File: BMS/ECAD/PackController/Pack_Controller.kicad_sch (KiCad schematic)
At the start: 0 parts

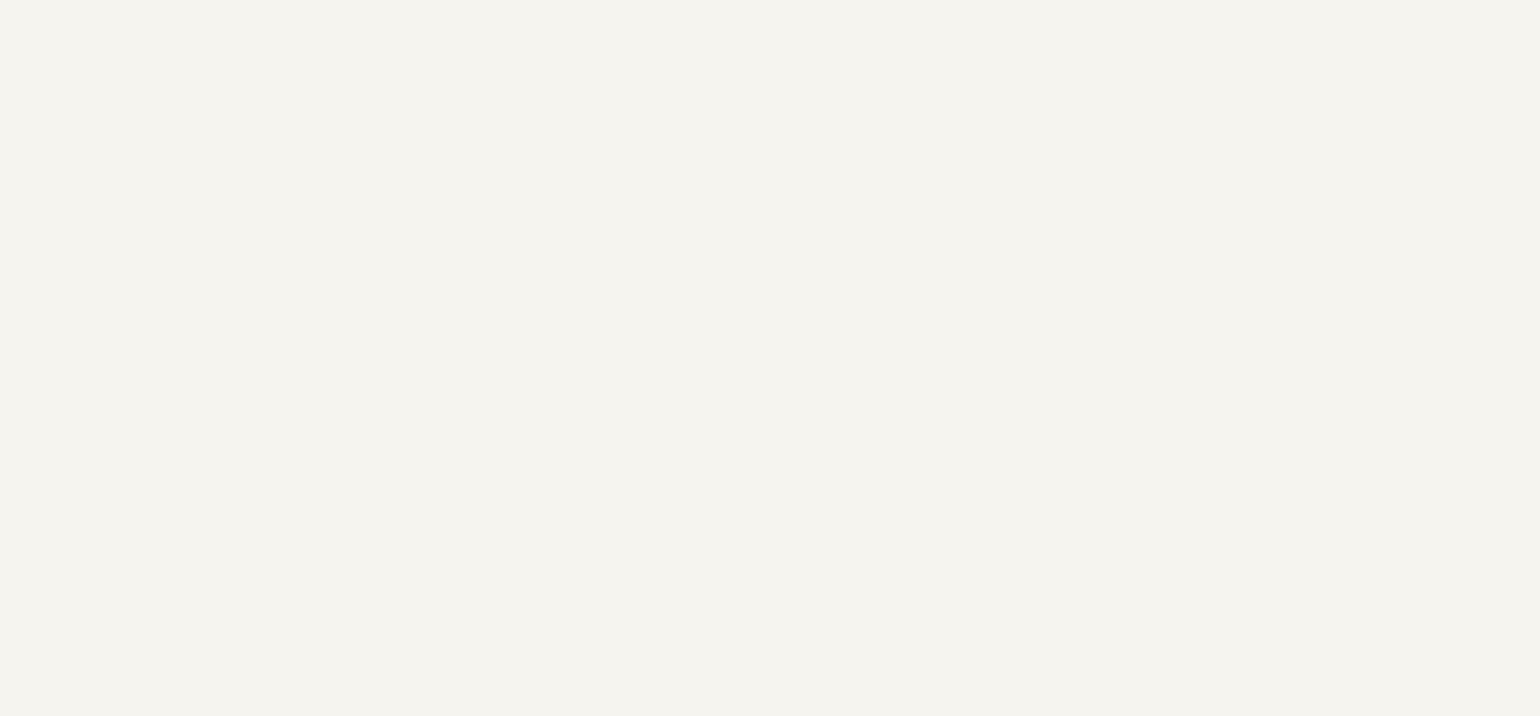
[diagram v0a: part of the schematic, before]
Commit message: did AIR monitoring circuit and started SDC CTRL / logik
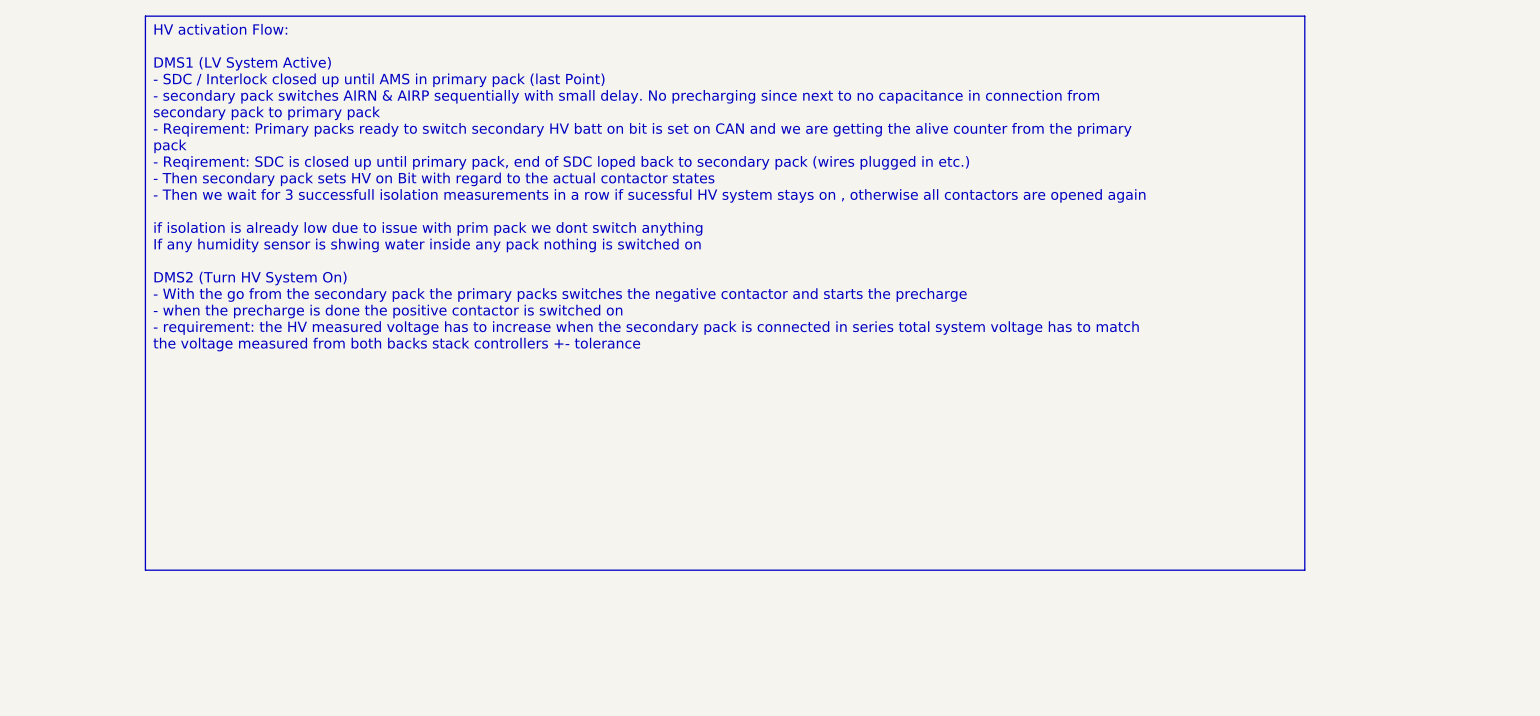
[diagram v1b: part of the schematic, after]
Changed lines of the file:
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@@
 		(company "Lukas Elektronik")
+	)
+	(text_box "HV activation Flow:\n\nDMS1 (LV System Active)\n- SDC / Interlock closed up until AMS in primary pack (last Point)\n- secondary pack switches AIRN & AIRP sequentially with small delay. No precharging since next to no capacitance in connection from secondary pack to primary pack\n- Reqirement: Primary packs ready to switch secondary HV batt on bit is set on CAN and we are getting the alive counter from the primary pack\n- Reqirement: SDC is closed up until primary pack, end of SDC loped back to secondary pack (wires plugged in etc.)\n- Then secondary pack sets HV on Bit with regard to the actual contactor states\n- Then we wait for 3 successfull isolation measurements in a row if sucessful HV system stays on , otherwise all contactors are opened again\n\nif isolation is already low due to issue with prim pack we dont switch anything\nIf any humidity sensor is shwing water inside any pack nothing is switched on\n\nDMS2 (Turn HV System On)\n- With the go from the secondary pack the primary packs switches the negative contactor and starts the precharge\n- when the precharge is done the positive contactor is switched on\n- requirement: the HV measured voltage has to increase when the secondary pack is connected in series total system voltage has to match the voltage measured from both backs stack controllers +- tolerance\n"
+		(exclude_from_sim no)
+		(at 317.5 10.16 0)
+		(size 143.51 68.58)
+		(margins 0.9525 0.9525 0.9525 0.9525)
+		(stroke
+			(width 0)
+			(type solid)
+		)
+		(fill
+			(type none)
+		)
+		(effects
+			(font
+				(size 1.27 1.27)
+			)
+			(justify left top)
+		)
 	)
 	(sheet

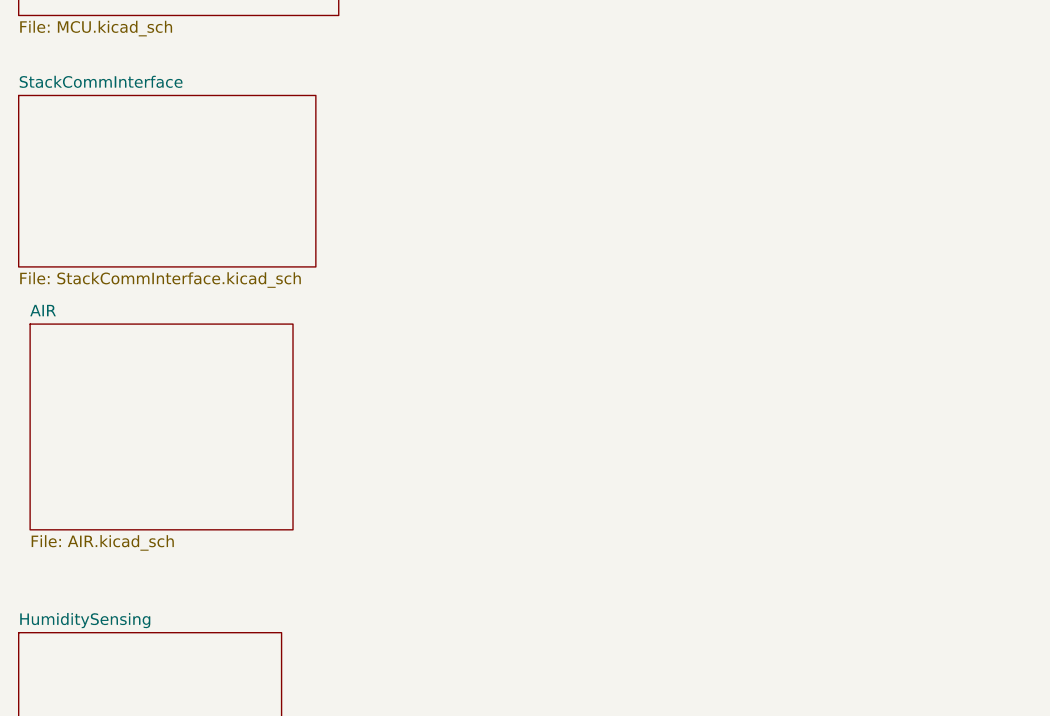
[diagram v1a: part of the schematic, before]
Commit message: IMD control circuit
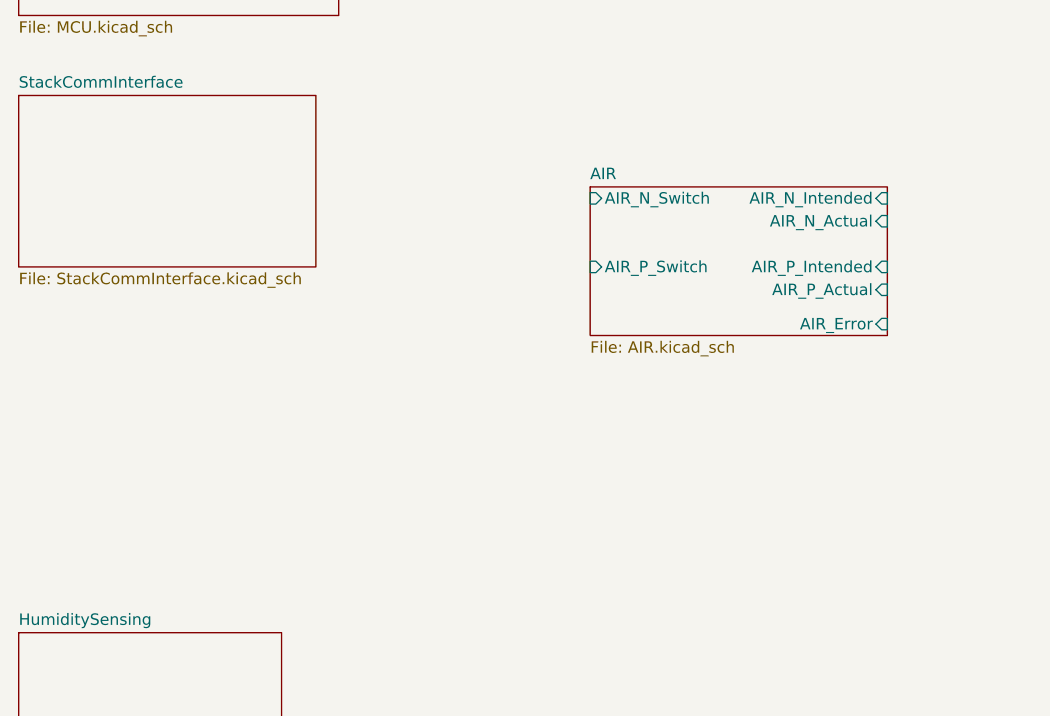
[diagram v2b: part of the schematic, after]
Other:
- sheet AIR ports: added AIR_Error, AIR_N_Actual, AIR_N_Intended, AIR_N_Switch, AIR_P_Actual, AIR_P_Intended, AIR_P_Switch; removed none
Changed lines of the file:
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@@
 	)
 	(sheet
-		(at 24.13 72.39)
-		(size 29.21 22.86)
+		(at 86.36 57.15)
+		(size 33.02 16.51)
 		(exclude_from_sim no)
 		(in_bom yes)
@@
 		)
 		(property "Sheetname" "AIR"
-			(at 24.13 71.6784 0)
+			(at 86.36 56.4384 0)
 			(effects
 				(font
@@
 		)
 		(property "Sheetfile" "AIR.kicad_sch"
-			(at 24.13 95.8346 0)
+			(at 86.36 74.2446 0)
 			(effects
 				(font
@@
 			)
 		)
+		(pin "AIR_N_Switch" input
+			(at 86.36 58.42 180)
+			(effects
+				(font
+					(size 1.27 1.27)
+				)
+				(justify left)
+			)
+		)
+		(pin "AIR_Error" input
+			(at 119.38 72.39 0)
+			(effects
+				(font
+					(size 1.27 1.27)
+				)
+				(justify right)
+			)
+		)
+		(pin "AIR_N_Actual" input
+			(at 119.38 60.96 0)
+			(effects
+				(font
+					(size 1.27 1.27)
+				)
+				(justify right)
+			)
+		)
+		(pin "AIR_N_Intended" input
+			(at 119.38 58.42 0)
+			(effects
+				(font
+					(size 1.27 1.27)
+				)
+				(justify right)
+			)
+		)
+		(pin "AIR_P_Actual" input
+			(at 119.38 68.58 0)
+			(effects
+				(font
+					(size 1.27 1.27)
+				)
+				(justify right)
+			)
+		)
+		(pin "AIR_P_Intended" input
+			(at 119.38 66.04 0)
+			(effects
+				(font
+					(size 1.27 1.27)
+				)
+				(justify right)
+			)
+		)
+		(pin "AIR_P_Switch" input
+			(at 86.36 66.04 180)
+			(effects
+				(font
+					(size 1.27 1.27)
+				)
+				(justify left)
+			)
+		)

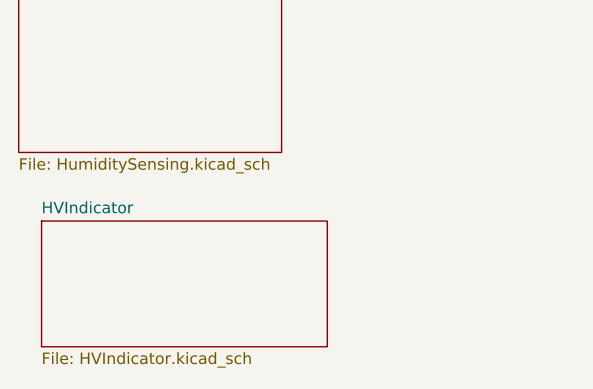
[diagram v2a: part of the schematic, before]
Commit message: add several subcomponent starts
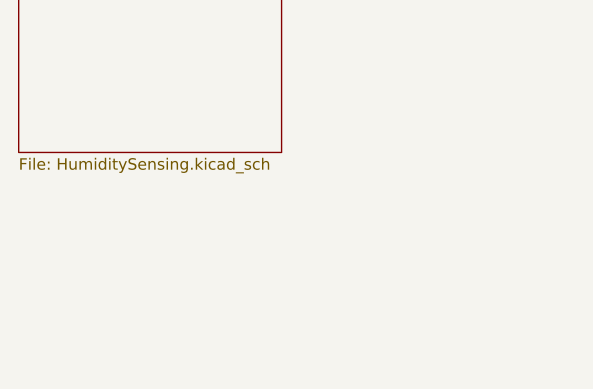
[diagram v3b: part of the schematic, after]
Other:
- removed sheet HVIndicator
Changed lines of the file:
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@@
-	)
-	(sheet
-		(at 25.4 134.62)
-		(size 31.75 13.97)
-		(exclude_from_sim no)
-		(in_bom yes)
-		(on_board yes)
-		(dnp no)
-		(fields_autoplaced yes)
-		(stroke
-			(width 0.1524)
-			(type solid)
-		)
-		(fill
-			(color 0 0 0 0.0000)
-		)
-		(property "Sheetname" "HVIndicator"
-			(at 25.4 133.9084 0)
-			(effects
-				(font
-					(size 1.27 1.27)
-				)
-				(justify left bottom)
-			)
-		)
-		(property "Sheetfile" "HVIndicator.kicad_sch"
-			(at 25.4 149.1746 0)
-			(effects
-				(font
-					(size 1.27 1.27)
-				)
-				(justify left top)
-			)
-		)
-		(instances
-			(project "Pack_Controller"
-				(path "/58a1c93e-baba-4d23-9191-955e00968735"
-					(page "5")
-				)
-			)
-		)
 	)
 	(sheet

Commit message: pack controller close to finished and startet pack controller
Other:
- added sheet Buzzer (Buzzer.kicad_sch)
- added sheet CAN (CAN.kicad_sch)
- added sheet HV_Measurement (HV_Measurement.kicad_sch)
- added sheet Precharge (Precharge.kicad_sch)
- added sheet TSAL_Logik (TSAL_Logik.kicad_sch)
- sheet HumiditySensing ports: added R_Leak1_ElecIn, R_Leak1_ElecOut, R_Leak1_Signal, R_Leak1_Supply, R_Leak2_ElecIn, R_Leak2_ElecOut, R_Leak2_Signal, R_Leak2_Supply; removed none
- sheet StackCommInterface ports: added ERRQ, ERRQ_Ioc_out, ERRQ_ext, ERRQ_ext_out, ERRQ_res, IFH_H, IFH_L, IFL_H, IFL_L, UART_HS_RX, UART_HS_TX, UART_LS_RX, UART_LS_TX, nSleep; removed none

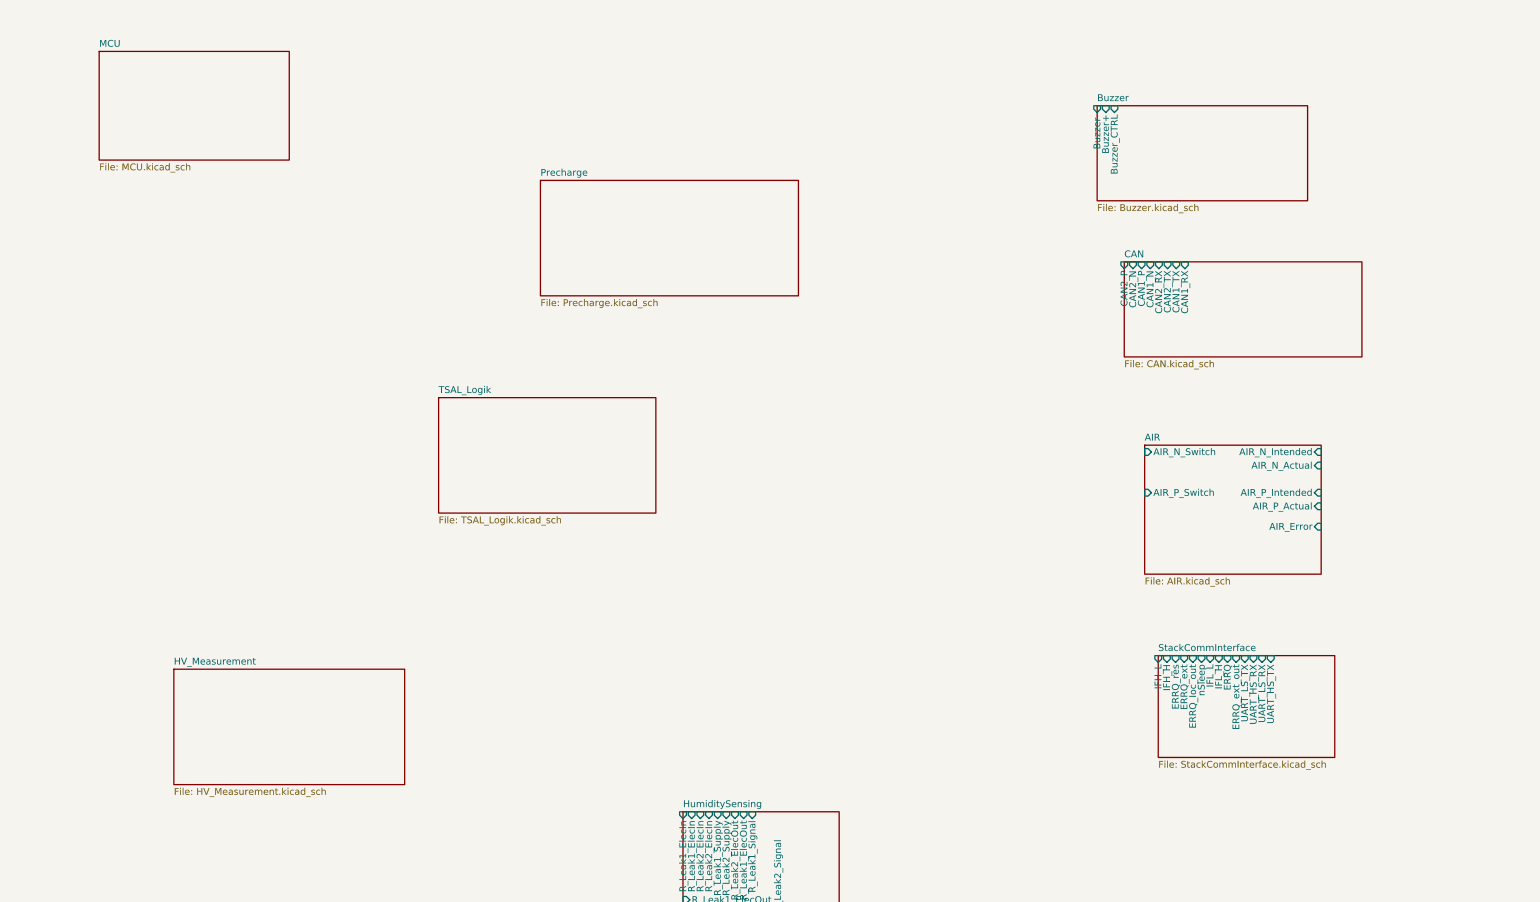
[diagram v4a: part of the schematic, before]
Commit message: finished schemativ of precharge
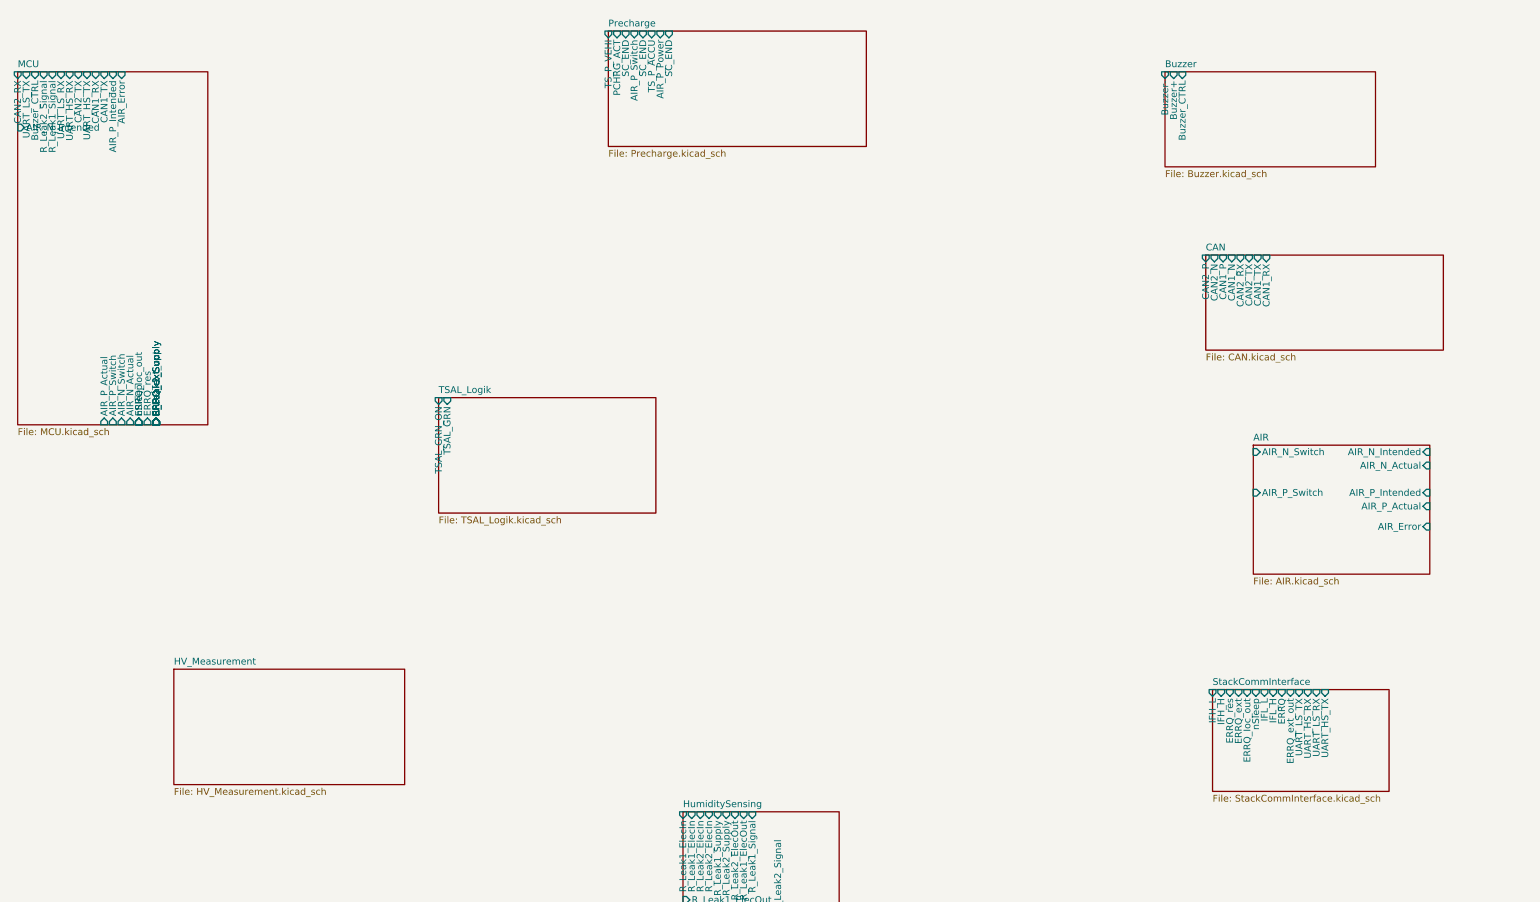
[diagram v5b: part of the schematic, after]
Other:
- sheet MCU ports: added AIR_Error, AIR_N_Actual, AIR_N_Intended, AIR_N_Switch, AIR_P_Actual, AIR_P_Intended, AIR_P_Switch, Buzzer_CTRL, CAN1_RX, CAN1_TX, CAN2_RX, CAN2_TX, ERRQ, ERRQ_Ioc_out, ERRQ_ext, ERRQ_ext_out, ERRQ_res, R_Leak1_Signal, R_Leak1_Supply, R_Leak2_Signal, R_Leak2_Supply, UART_HS_RX, UART_HS_TX, UART_LS_RX, UART_LS_TX, nSleep; removed none
- sheet Precharge ports: added AIR_P_Power, AIR_P_Switch, PCHRG_ACT, SC_END, TS_P_ACCU, TS_P_VEHI; removed none
- sheet TSAL_Logik ports: added TSAL_GRN, TSAL_GRN_ON; removed none
- title: PackController_Overview -> PackController
